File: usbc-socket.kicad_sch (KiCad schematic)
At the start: 10 parts, among them J10 USB-C_USB4105-GF-A, Q16 PJA3441, Q17 DTC014T_SOT-416, U59 82400152, U60 82400152

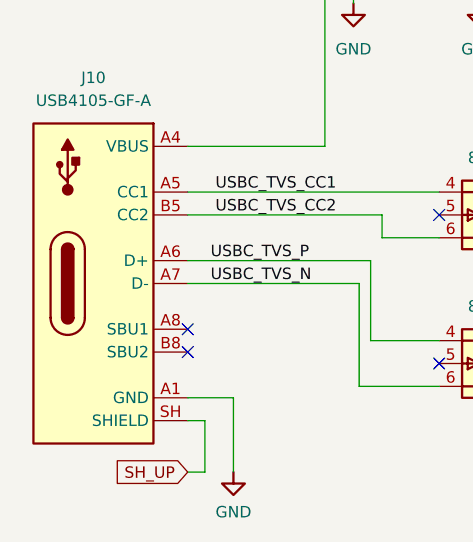
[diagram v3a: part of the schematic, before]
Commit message: [#56935] Update symbol/footprint links; Migrate to KiCad 7
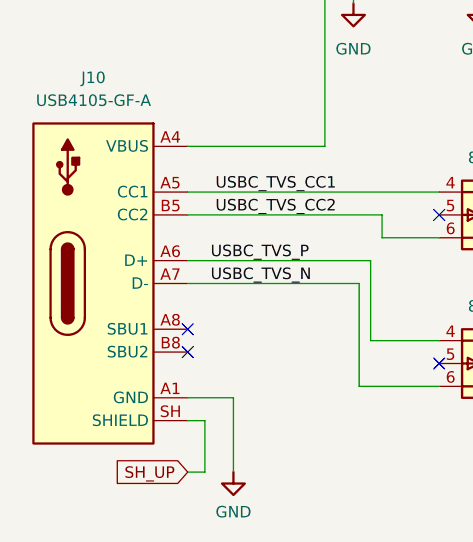
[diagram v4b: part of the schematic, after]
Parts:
- C231: footprint kria-k26-devboard-footprints:C_0402_1005Metric -> antmicro-footprints:C_0402_1005Metric; symbol kria-k26-devboard:C_100n_50V_0402 -> antmicroCapacitorsmisc:C_100n_50V_0402
- D26: footprint kria-k26-devboard-footprints:SOD-123FL -> antmicro-footprints:SOD-123FL; symbol kria-k26-devboard:SMF4L15CA -> antmicroTVSDiodes:SMF4L15CA
- J10: footprint kria-k26-devboard-footprints:USB-C_GCT_USB4105-GF-A -> antmicro-footprints:USB-C_Receptacle_GCT_USB4105-GF-A; symbol kria-k26-devboard:USB-C_USB4105-GF-A -> antmicroUSBConnectors:USB-C_GCT_USB4105-GF-A
- Q16: footprint kria-k26-devboard-footprints:SOT-23-3 -> antmicro-footprints:SOT-23-3; symbol kria-k26-devboard:PJA3441 -> antmicroTransistorsFETsMOSFETsSingle:PJA3441
- Q17: footprint kria-k26-devboard-footprints:SOT-416 -> antmicro-footprints:SOT-416; symbol kria-k26-devboard:DTC014T_SOT-416 -> antmicroTransistorsBipolarSingle:DTC014T_SOT-416
- R149: footprint kria-k26-devboard-footprints:R_0402_1005Metric -> antmicro-footprints:R_0402_1005Metric; symbol kria-k26-devboard:R_100k_0402 -> antmicroResistors0402:R_100k_0402
- TP44, TP45: footprint kria-k26-devboard-footprints:TP_SMD_0.75mm -> antmicro-footprints:TP_SMD_0.75mm; symbol kria-k26-devboard:TP_0.75mm_SMD -> antmicroTestPoints:TP_0.75mm_SMD
- U59, U60: footprint kria-k26-devboard-footprints:SOT-563 -> antmicro-footprints:SOT-563; symbol kria-k26-devboard:82400152 -> antmicroTVSDiodes:82400152

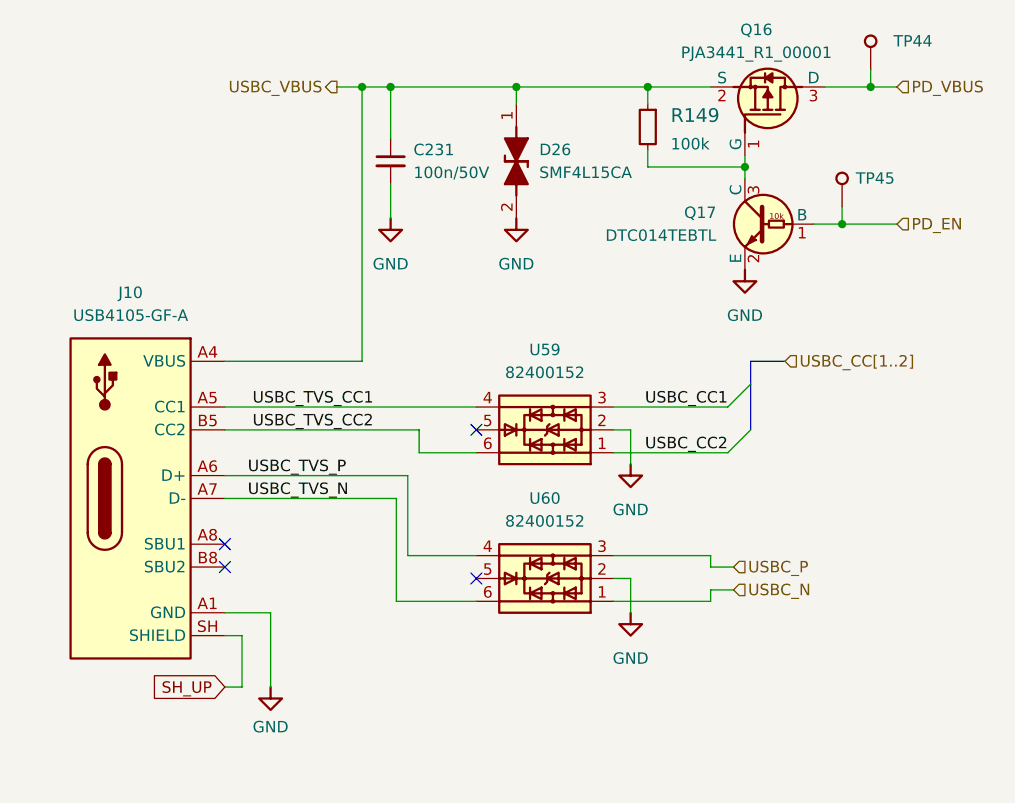
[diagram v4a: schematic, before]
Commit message: [#56935] Fix missing highlights in OHP
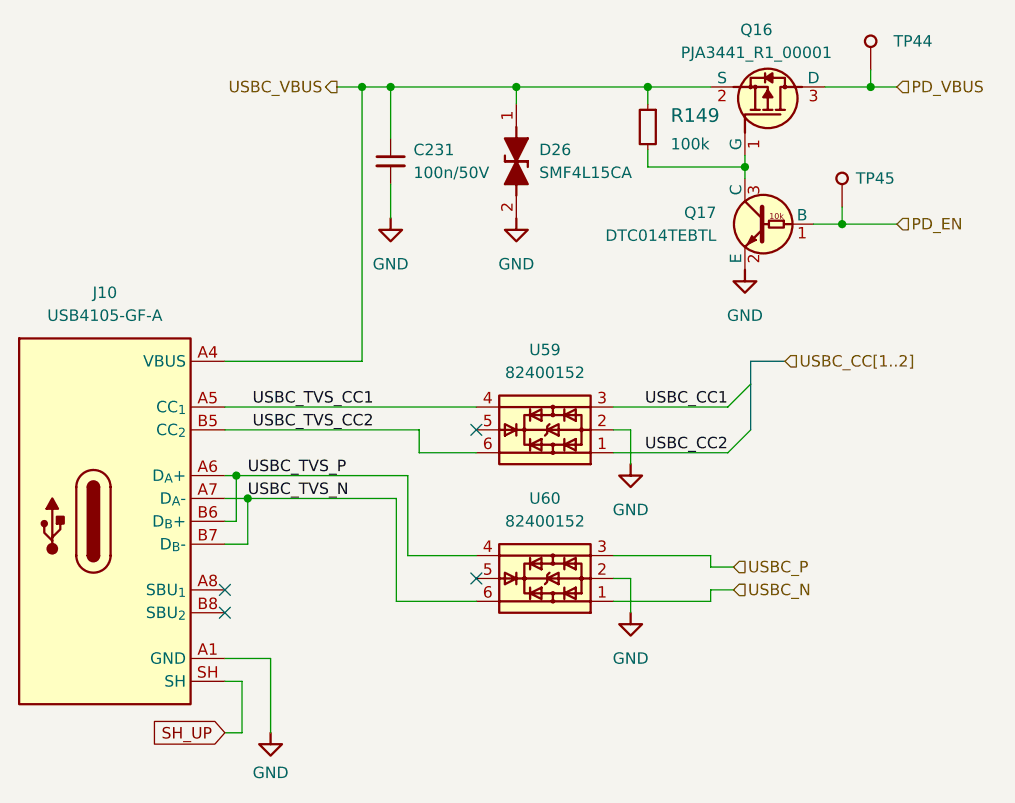
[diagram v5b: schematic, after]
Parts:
- J10: value USB-C_USB4105-GF-A -> USB-C_GCT_USB4105-GF-A; VSD_Class (none) -> USB-C
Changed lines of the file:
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@@
   (junction (at 183.515 57.15) (diameter 0) (color 0 0 0 0)
   )
+  (junction (at 114.3 102.87) (diameter 0) (color 0 0 0 0)
+  )
   (junction (at 130.175 57.15) (diameter 0) (color 0 0 0 0)
   )
@@
   (junction (at 180.34 72.39) (diameter 0) (color 0 0 0 0)
   )
+  (junction (at 113.03 100.33) (diameter 0) (color 0 0 0 0)
+  )
   (junction (at 158.75 57.15) (diameter 0) (color 0 0 0 0)
   )
@@
   )
   (no_connect (at 139.7 111.76))
-  (no_connect (at 111.76 107.95))
-  (no_connect (at 111.76 110.49))
+  (no_connect (at 111.76 113.03))
+  (no_connect (at 111.76 115.57))
   (no_connect (at 139.7 95.25))
   (bus_entry (at 170.18 90.17) (size -2.54 2.54)
@@
     (stroke (width 0) (type default))
   )
-  (wire (pts (xy 116.84 115.57) (xy 116.84 123.825))
+  (wire (pts (xy 116.84 120.65) (xy 116.84 128.905))
     (stroke (width 0) (type default))
   )
@@
     (stroke (width 0) (type default))
   )
-  (wire (pts (xy 111.76 123.825) (xy 113.665 123.825))
+  (wire (pts (xy 111.76 128.905) (xy 113.665 128.905))
     (stroke (width 0) (type default))
   )
@@
     (stroke (width 0) (type default))
   )
-  (wire (pts (xy 113.665 123.825) (xy 113.665 118.11))
+  (wire (pts (xy 113.665 128.905) (xy 113.665 123.19))
     (stroke (width 0) (type default))
   )
@@
     (stroke (width 0) (type default))
   )
-  (wire (pts (xy 111.76 100.33) (xy 132.08 100.33))
+  (wire (pts (xy 111.76 100.33) (xy 113.03 100.33))
     (stroke (width 0) (type default))
   )
@@
     (stroke (width 0) (type default))
   )
-  (wire (pts (xy 113.665 118.11) (xy 111.76 118.11))
+  (wire (pts (xy 113.665 123.19) (xy 111.76 123.19))
     (stroke (width 0) (type default))
   )
@@
     (stroke (width 0) (type default))
   )
-  (wire (pts (xy 111.76 102.87) (xy 130.81 102.87))
+  (wire (pts (xy 111.76 102.87) (xy 114.3 102.87))
+    (stroke (width 0) (type default))
+  )
+  (wire (pts (xy 111.76 107.95) (xy 114.3 107.95))
+    (stroke (width 0) (type default))
+  )
+  (wire (pts (xy 113.03 105.41) (xy 113.03 100.33))
     (stroke (width 0) (type default))
   )
@@
     (stroke (width 0) (type default))
   )
-  (wire (pts (xy 116.84 115.57) (xy 111.76 115.57))
+  (wire (pts (xy 116.84 120.65) (xy 111.76 120.65))
+    (stroke (width 0) (type default))
+  )
+  (wire (pts (xy 113.03 100.33) (xy 132.08 100.33))
     (stroke (width 0) (type default))
   )
@@
     (stroke (width 0) (type default))
   )
+  (wire (pts (xy 114.3 102.87) (xy 130.81 102.87))
+    (stroke (width 0) (type default))
+  )
+  (wire (pts (xy 111.76 105.41) (xy 113.03 105.41))
+    (stroke (width 0) (type default))
+  )
   (wire (pts (xy 154.94 114.3) (xy 165.735 114.3))
+    (stroke (width 0) (type default))
+  )
+  (wire (pts (xy 114.3 107.95) (xy 114.3 102.87))
     (stroke (width 0) (type default))
   )
@@
     (effects (font (size 1.27 1.27)) (justify left bottom))
   )
-  (global_label "SH_UP" (shape input) (at 111.76 123.825 180) (fields_autoplaced)
+  (global_label "SH_UP" (shape input) (at 111.76 128.905 180) (fields_autoplaced)
     (effects (font (size 1.27 1.27)) (justify right))
-    (property "Intersheetrefs" "${INTERSHEET_REFS}" (at 103.3277 123.9044 0)
+    (property "Intersheetrefs" "${INTERSHEET_REFS}" (at 103.3277 128.9844 0)
       (effects (font (size 1.27 1.27)) (justify right) hide)
     )
@@
     )
   )
-  (symbol (lib_id "antmicropower:GND") (at 116.84 123.825 0) (unit 1)
+  (symbol (lib_id "antmicropower:GND") (at 116.84 128.905 0) (unit 1)
     (in_bom yes) (on_board yes) (dnp no) (fields_autoplaced)
-    (property "Reference" "#PWR0391" (at 116.84 130.175 0)
+    (property "Reference" "#PWR0391" (at 116.84 135.255 0)
       (effects (font (size 1.27 1.27)) hide)
     )
-    (property "Value" "GND" (at 116.84 128.27 0)
+    (property "Value" "GND" (at 116.84 133.35 0)
       (effects (font (size 1.27 1.27)))
     )
-    (property "Footprint" "" (at 125.73 131.445 0)
+    (property "Footprint" "" (at 125.73 136.525 0)
       (effects (font (size 1.27 1.27) (thickness 0.15)) (justify left bottom) hide)
     )
-    (property "Datasheet" "" (at 125.73 136.525 0)
+    (property "Datasheet" "" (at 125.73 141.605 0)
       (effects (font (size 1.27 1.27) (thickness 0.15)) (justify left bottom) hide)
     )
-    (property "Author" "Antmicro" (at 125.73 131.445 0)
+    (property "Author" "Antmicro" (at 125.73 136.525 0)
       (effects (font (size 1.27 1.27) (thickness 0.15)) (justify left bottom) hide)
     )
-    (property "License" "Apache-2.0" (at 125.73 133.985 0)
+    (property "License" "Apache-2.0" (at 125.73 139.065 0)
       (effects (font (size 1.27 1.27) (thickness 0.15)) (justify left bottom) hide)
     )
@@
     )
   )
-  (symbol (lib_id "antmicroUSBConnectors:USB-C_GCT_USB4105-GF-A") (at 111.76 87.63 0) (mirror y) (unit 1)
+  (symbol (lib_id "antmicroUSBConnectors:USB-C_GCT_USB4105-GF-A") (at 111.76 87.63 0) (unit 1)
     (in_bom yes) (on_board yes) (dnp no) (fields_autoplaced)
-    (property "Reference" "J10" (at 101.2825 80.01 0)
+    (property "Reference" "J10" (at 98.425 80.01 0)
       (effects (font (size 1.27 1.27)))
     )
-    (property "Value" "USB-C_USB4105-GF-A" (at 101.2825 81.915 0)
+    (property "Value" "USB-C_GCT_USB4105-GF-A" (at 122.2375 81.915 0)
       (effects (font (size 1.27 1.27) (thickness 0.15)) hide)
     )
-    (property "Footprint" "antmicro-footprints:USB-C_Receptacle_GCT_USB4105-GF-A" (at 128.27 81.28 0)
+    (property "Footprint" "antmicro-footprints:USB-C_Receptacle_GCT_USB4105-GF-A" (at 95.25 81.28 0)
       (effects (font (size 1.27 1.27) (thickness 0.15)) (justify left bottom) hide)
     )
@@
       (effects (font (size 1.27 1.27) (thickness 0.15)) (justify left bottom) hide)
     )
-    (property "Manufacturer" "GCT" (at 128.27 78.74 0)
+    (property "Manufacturer" "GCT" (at 95.25 78.74 0)
       (effects (font (size 1.27 1.27) (thickness 0.15)) (justify left bottom) hide)
     )
-    (property "MPN" "USB4105-GF-A" (at 101.2825 82.55 0)
+    (property "MPN" "USB4105-GF-A" (at 98.425 82.55 0)
       (effects (font (size 1.27 1.27) (thickness 0.15)))
     )
-    (property "Author" "Antmicro" (at 73.66 105.41 0)
+    (property "Author" "Antmicro" (at 149.86 105.41 0)
       (effects (font (size 1.27 1.27) (thickness 0.15)) (justify left bottom) hide)
     )
-    (property "License" "Apache-2.0" (at 73.66 107.95 0)
+    (property "License" "Apache-2.0" (at 149.86 107.95 0)
       (effects (font (size 1.27 1.27) (thickness 0.15)) (justify left bottom) hide)
     )
+    (property "VSD_Class" "USB-C" (at 149.86 110.49 0)
+      (effects (font (size 1.27 1.27)) (justify left bottom) hide)
+    )
     (pin "A1")

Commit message: [#56935] Loclib
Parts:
- C231: footprint antmicro-footprints:C_0402_1005Metric -> kria-k26-devboard-footprints:C_0402_1005Metric; symbol antmicroCapacitorsmisc:C_100n_50V_0402 -> kria-k26-devboard:C_100n_50V_0402
- D26: footprint antmicro-footprints:SOD-123FL -> kria-k26-devboard-footprints:SOD-123FL; symbol antmicroTVSDiodes:SMF4L15CA -> kria-k26-devboard:SMF4L15CA
- J10: footprint antmicro-footprints:USB-C_Receptacle_GCT_USB4105-GF-A -> kria-k26-devboard-footprints:USB-C_Receptacle_GCT_USB4105-GF-A; symbol antmicroUSBConnectors:USB-C_GCT_USB4105-GF-A -> kria-k26-devboard:USB-C_GCT_USB4105-GF-A
- Q16: footprint antmicro-footprints:SOT-23-3 -> kria-k26-devboard-footprints:SOT-23-3; symbol antmicroTransistorsFETsMOSFETsSingle:PJA3441 -> kria-k26-devboard:PJA3441
- Q17: footprint antmicro-footprints:SOT-416 -> kria-k26-devboard-footprints:SOT-416; symbol antmicroTransistorsBipolarSingle:DTC014T_SOT-416 -> kria-k26-devboard:DTC014T_SOT-416
- R149: footprint antmicro-footprints:R_0402_1005Metric -> kria-k26-devboard-footprints:R_0402_1005Metric; symbol antmicroResistors0402:R_100k_0402 -> kria-k26-devboard:R_100k_0402
- TP44, TP45: footprint antmicro-footprints:TP_SMD_0.75mm -> kria-k26-devboard-footprints:TP_SMD_0.75mm; symbol antmicroTestPoints:TP_0.75mm_SMD -> kria-k26-devboard:TP_0.75mm_SMD
- U59, U60: footprint antmicro-footprints:SOT-563 -> kria-k26-devboard-footprints:SOT-563; symbol antmicroTVSDiodes:82400152 -> kria-k26-devboard:82400152
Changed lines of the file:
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@@
     (effects (font (size 1.27 1.27)) (justify left))
   )
-  (symbol (lib_id "antmicroTVSDiodes:SMF4L15CA") (at 144.145 59.055 270) (unit 1)
+  (symbol (lib_id "kria-k26-devboard:SMF4L15CA") (at 144.145 59.055 270) (unit 1)
     (in_bom yes) (on_board yes) (dnp no) (fields_autoplaced)
     (property "Reference" "D26" (at 146.685 64.1349 90)
@@
       (effects (font (size 1.27 1.27) (thickness 0.15)) (justify left) hide)
     )
-    (property "Footprint" "antmicro-footprints:SOD-123FL" (at 144.145 59.055 0)
+    (property "Footprint" "kria-k26-devboard-footprints:SOD-123FL" (at 144.145 59.055 0)
       (effects (font (size 1.27 1.27) (thickness 0.15)) (justify left bottom) hide)
     )
@@
     )
   )
-  (symbol (lib_id "antmicropower:GND") (at 116.84 128.905 0) (unit 1)
+  (symbol (lib_id "kria-k26-devboard:GND") (at 116.84 128.905 0) (unit 1)
     (in_bom yes) (on_board yes) (dnp no) (fields_autoplaced)
     (property "Reference" "#PWR0391" (at 116.84 135.255 0)
@@
     )
   )
-  (symbol (lib_id "antmicroUSBConnectors:USB-C_GCT_USB4105-GF-A") (at 111.76 87.63 0) (unit 1)
+  (symbol (lib_id "kria-k26-devboard:USB-C_GCT_USB4105-GF-A") (at 111.76 87.63 0) (unit 1)
     (in_bom yes) (on_board yes) (dnp no) (fields_autoplaced)
     (property "Reference" "J10" (at 98.425 80.01 0)
@@
       (effects (font (size 1.27 1.27) (thickness 0.15)) hide)
     )
-    (property "Footprint" "antmicro-footprints:USB-C_Receptacle_GCT_USB4105-GF-A" (at 95.25 81.28 0)
+    (property "Footprint" "kria-k26-devboard-footprints:USB-C_Receptacle_GCT_USB4105-GF-A" (at 95.25 81.28 0)
       (effects (font (size 1.27 1.27) (thickness 0.15)) (justify left bottom) hide)
     )
@@
     )
   )
-  (symbol (lib_id "antmicropower:GND") (at 144.145 71.755 0) (unit 1)
+  (symbol (lib_id "kria-k26-devboard:GND") (at 144.145 71.755 0) (unit 1)
     (in_bom yes) (on_board yes) (dnp no) (fields_autoplaced)
     (property "Reference" "#PWR0392" (at 144.145 78.105 0)
@@
     )
   )
-  (symbol (lib_id "antmicroCapacitorsmisc:C_100n_50V_0402") (at 130.175 62.865 270) (unit 1)
+  (symbol (lib_id "kria-k26-devboard:C_100n_50V_0402") (at 130.175 62.865 270) (unit 1)
     (in_bom yes) (on_board yes) (dnp no) (fields_autoplaced)
     (property "Reference" "C231" (at 132.715 64.1412 90)
@@
       (effects (font (size 1.27 1.27) (thickness 0.15)) (justify left bottom) hide)
     )
-    (property "Footprint" "antmicro-footprints:C_0402_1005Metric" (at 130.175 62.865 0)
+    (property "Footprint" "kria-k26-devboard-footprints:C_0402_1005Metric" (at 130.175 62.865 0)
       (effects (font (size 1.27 1.27) (thickness 0.15)) (justify left bottom) hide)
     )
@@
     )
   )
-  (symbol (lib_id "antmicroTVSDiodes:82400152") (at 154.94 114.3 180) (unit 1)
+  (symbol (lib_id "kria-k26-devboard:82400152") (at 154.94 114.3 180) (unit 1)
     (in_bom yes) (on_board yes) (dnp no) (fields_autoplaced)
     (property "Reference" "U60" (at 147.32 102.87 0)
@@
       (effects (font (size 1.27 1.27) (thickness 0.15)))
     )
-    (property "Footprint" "antmicro-footprints:SOT-563" (at 154.94 109.22 0)
+    (property "Footprint" "kria-k26-devboard-footprints:SOT-563" (at 154.94 109.22 0)
       (effects (font (size 1.27 1.27) (thickness 0.15)) (justify left bottom) hide)
     )
@@
     )
   )
-  (symbol (lib_id "antmicroTransistorsBipolarSingle:DTC014T_SOT-416") (at 177.165 72.39 0) (mirror y) (unit 1)
+  (symbol (lib_id "kria-k26-devboard:DTC014T_SOT-416") (at 177.165 72.39 0) (mirror y) (unit 1)
     (in_bom yes) (on_board yes) (dnp no) (fields_autoplaced)
     (property "Reference" "Q17" (at 166.37 71.1199 0)
@@
       (effects (font (size 1.27 1.27) (thickness 0.15)) (justify left) hide)
     )
-    (property "Footprint" "antmicro-footprints:SOT-416" (at 172.085 80.01 0)
+    (property "Footprint" "kria-k26-devboard-footprints:SOT-416" (at 172.085 80.01 0)
       (effects (font (size 1.27 1.27) (thickness 0.15)) (justify left bottom) hide)
     )
@@
     )
   )
-  (symbol (lib_id "antmicroTestPoints:TP_0.75mm_SMD") (at 183.515 55.245 90) (unit 1)
+  (symbol (lib_id "kria-k26-devboard:TP_0.75mm_SMD") (at 183.515 55.245 90) (unit 1)
     (in_bom yes) (on_board yes) (dnp no) (fields_autoplaced)
     (property "Reference" "TP44" (at 186.055 52.0699 90)
@@
       (effects (font (size 1.27 1.27) (thickness 0.15)) (justify left bottom) hide)
     )
-    (property "Footprint" "antmicro-footprints:TP_SMD_0.75mm" (at 178.435 50.165 0)
+    (property "Footprint" "kria-k26-devboard-footprints:TP_SMD_0.75mm" (at 178.435 50.165 0)
       (effects (font (size 1.27 1.27) (thickness 0.15)) (justify left bottom) hide)
     )
@@
     )
   )
-  (symbol (lib_id "antmicroTestPoints:TP_0.75mm_SMD") (at 180.34 70.485 90) (unit 1)
+  (symbol (lib_id "kria-k26-devboard:TP_0.75mm_SMD") (at 180.34 70.485 90) (unit 1)
     (in_bom yes) (on_board yes) (dnp no) (fields_autoplaced)
     (property "Reference" "TP45" (at 181.864 67.3099 90)
@@
       (effects (font (size 1.27 1.27) (thickness 0.15)) (justify left bottom) hide)
     )
-    (property "Footprint" "antmicro-footprints:TP_SMD_0.75mm" (at 175.26 65.405 0)
+    (property "Footprint" "kria-k26-devboard-footprints:TP_SMD_0.75mm" (at 175.26 65.405 0)
       (effects (font (size 1.27 1.27) (thickness 0.15)) (justify left bottom) hide)
     )
@@
     )
   )
-  (symbol (lib_id "antmicropower:GND") (at 156.845 115.57 0) (mirror y) (unit 1)
+  (symbol (lib_id "kria-k26-devboard:GND") (at 156.845 115.57 0) (mirror y) (unit 1)
     (in_bom yes) (on_board yes) (dnp no) (fields_autoplaced)
     (property "Reference" "#PWR0395" (at 156.845 121.92 0)
@@
     )
   )
-  (symbol (lib_id "antmicroTVSDiodes:82400152") (at 154.94 97.79 180) (unit 1)
+  (symbol (lib_id "kria-k26-devboard:82400152") (at 154.94 97.79 180) (unit 1)
     (in_bom yes) (on_board yes) (dnp no) (fields_autoplaced)
     (property "Reference" "U59" (at 147.32 86.36 0)
@@
       (effects (font (size 1.27 1.27) (thickness 0.15)))
     )
-    (property "Footprint" "antmicro-footprints:SOT-563" (at 154.94 92.71 0)
+    (property "Footprint" "kria-k26-devboard-footprints:SOT-563" (at 154.94 92.71 0)
       (effects (font (size 1.27 1.27) (thickness 0.15)) (justify left bottom) hide)
     )
@@
     )
   )
-  (symbol (lib_id "antmicropower:GND") (at 156.845 99.06 0) (unit 1)
+  (symbol (lib_id "kria-k26-devboard:GND") (at 156.845 99.06 0) (unit 1)
     (in_bom yes) (on_board yes) (dnp no) (fields_autoplaced)
     (property "Reference" "#PWR0393" (at 156.845 105.41 0)
@@
     )
   )
-  (symbol (lib_id "antmicroTransistorsFETsMOSFETsSingle:PJA3441") (at 169.545 64.77 270) (mirror x) (unit 1)
+  (symbol (lib_id "kria-k26-devboard:PJA3441") (at 169.545 64.77 270) (mirror x) (unit 1)
     (in_bom yes) (on_board yes) (dnp no)
     (property "Reference" "Q16" (at 170.815 50.8 90)
@@
       (effects (font (size 1.27 1.27) (thickness 0.15)) hide)
     )
-    (property "Footprint" "antmicro-footprints:SOT-23-3" (at 169.545 64.77 0)
+    (property "Footprint" "kria-k26-devboard-footprints:SOT-23-3" (at 169.545 64.77 0)
       (effects (font (size 1.27 1.27) (thickness 0.15)) (justify left bottom) hide)
     )
@@
     )
   )
-  (symbol (lib_id "antmicroResistors0402:R_100k_0402") (at 158.75 59.055 270) (unit 1)
+  (symbol (lib_id "kria-k26-devboard:R_100k_0402") (at 158.75 59.055 270) (unit 1)
     (in_bom yes) (on_board yes) (dnp no) (fields_autoplaced)
     (property "Reference" "R149" (at 161.29 60.325 90)
@@
       (effects (font (size 1.27 1.27) (thickness 0.15)) (justify left bottom) hide)
     )
-    (property "Footprint" "antmicro-footprints:R_0402_1005Metric" (at 163.83 64.135 0)
+    (property "Footprint" "kria-k26-devboard-footprints:R_0402_1005Metric" (at 163.83 64.135 0)
       (effects (font (size 1.27 1.27) (thickness 0.15)) (justify left bottom) hide)
     )
@@
     )
   )
-  (symbol (lib_id "antmicropower:GND") (at 169.545 77.47 0) (unit 1)
+  (symbol (lib_id "kria-k26-devboard:GND") (at 169.545 77.47 0) (unit 1)
     (in_bom yes) (on_board yes) (dnp no) (fields_autoplaced)
     (property "Reference" "#PWR0394" (at 169.545 83.82 0)
@@
     )
   )
-  (symbol (lib_id "antmicropower:GND") (at 130.175 71.755 0) (unit 1)
+  (symbol (lib_id "kria-k26-devboard:GND") (at 130.175 71.755 0) (unit 1)
     (in_bom yes) (on_board yes) (dnp no) (fields_autoplaced)
     (property "Reference" "#PWR0103" (at 130.175 78.105 0)
